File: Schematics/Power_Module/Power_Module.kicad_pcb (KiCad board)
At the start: 4 copper layers, 69.5 x 60 mm, 130 parts, among them J1 ScrewSwitch, J2 Battery, J3 ScrewSwitch, J4 GSE, J5 USB_C_Female_USB2_Small, J6 SWD_B, J7 Stack Male Edge Connector, Q1 AO4447A, Q2 TSM2309CX, Q3 DMN6040SSD-13, SW1 SW_STM_RESET, SW2 SW_STM_BOOT_MODE, U1 TPS61175PWPR, U10 LM66100DCKR, U11 LM66100DCKR, U12 AMS1117-3.3, U13 CP2102N-A02-GQFN20R, U14 STM32F103CBT6, U15 ISO1044BDR, U16 W25Q128JVS, U2 LM74700QDBVRQ1, U3 LM74700QDBVRQ1, U4 ACS37041KLHBLT-010B3, U5 ACS37041KLHBLT-010B5, U6 INA181A2, U7 LMR51430XDDCR, U8 LMR51430XDDCR, U9 LM66100DCKR, Y1 X322516MMB4SI

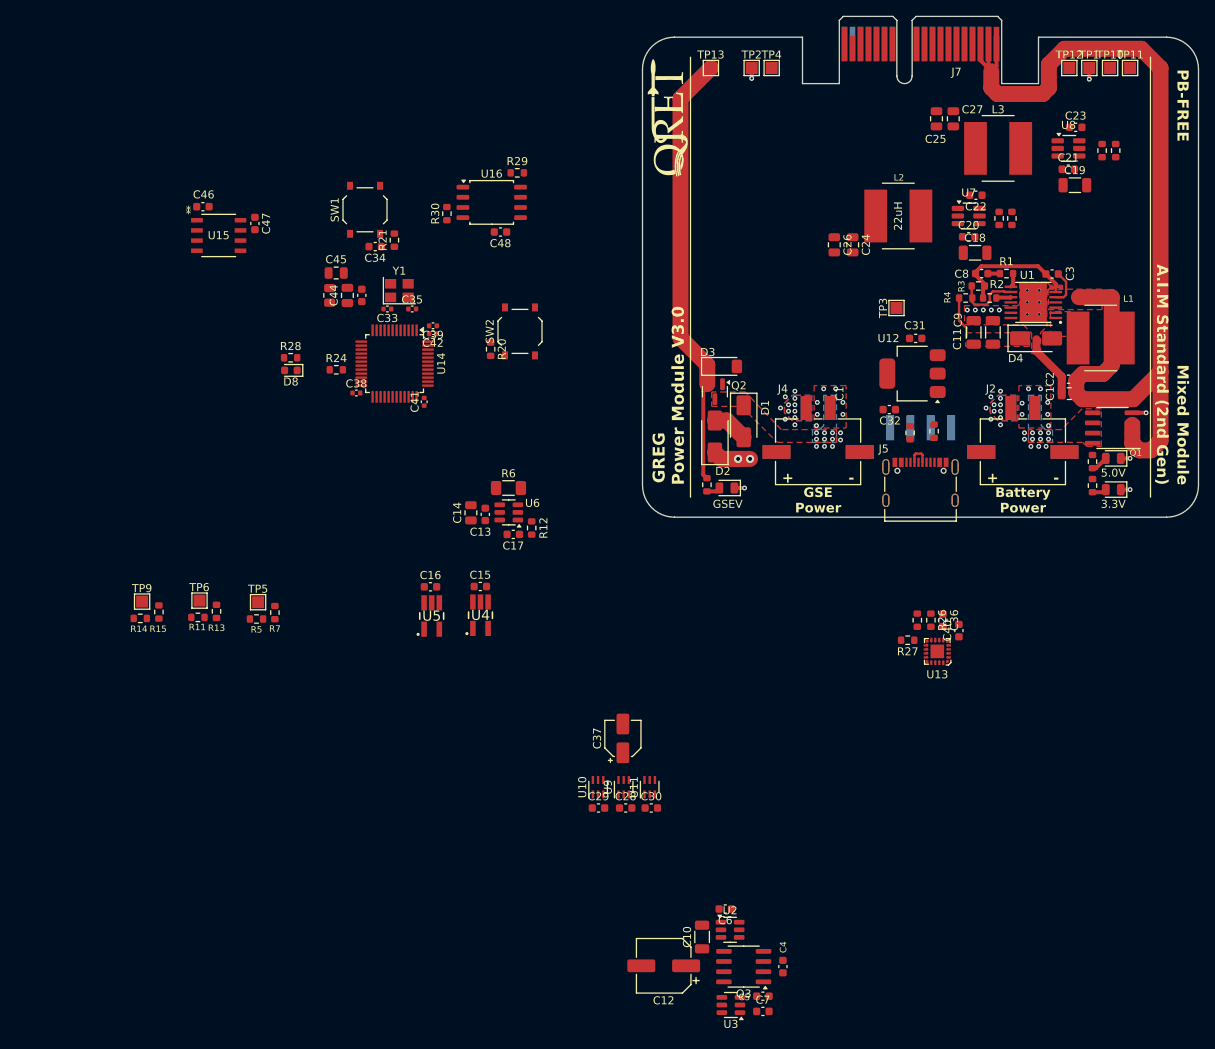
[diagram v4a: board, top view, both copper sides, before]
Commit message: continueing layout, confirmed all devices will fix  - need to add bulk rail caps  - fixed issue in oring logic
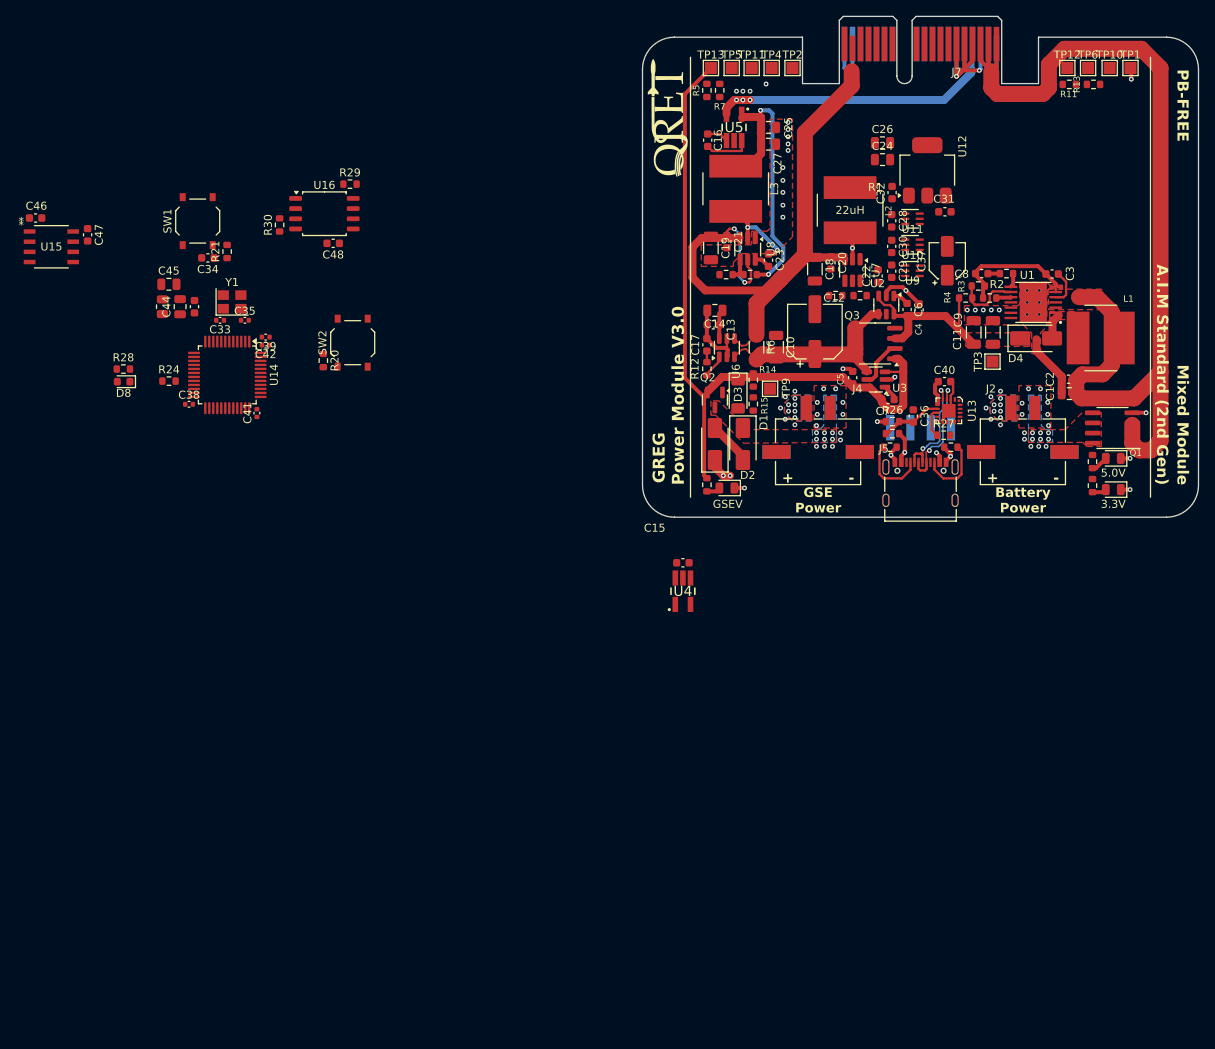
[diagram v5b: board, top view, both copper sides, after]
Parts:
- moved TP6 129.5 mm to (185.9, 43.6)
- moved R13 127.9 mm to (186.6, 45.6), turned to 0 degrees
- moved R11 127.7 mm to (183.6, 45.6)
- moved TP5 89.2 mm to (141.4, 43.6)
- moved R5 86.8 mm to (138.3, 46.4), turned to 90 degrees
- moved R7 85.7 mm to (139.9, 46.4)
- moved C4 83.8 mm to (164.8, 73.8), turned to -90 degrees
- moved TP9 82.9 mm to (146.2, 83.7), turned to 180 degrees
- moved R14 82.2 mm to (144.1, 82.6), turned to 90 degrees
- moved C12 81.5 mm to (151.8, 76.5), turned to 90 degrees
- moved C28 80.6 mm to (161.4, 62.7), turned to -90 degrees
- moved U2 80.5 mm to (160.7, 73.2), turned to -90 degrees
- moved U3 80.3 mm to (159.4, 82.5)
- moved U9 79.7 mm to (164.0, 62.5), turned to 0 degrees
- moved Q3 79.6 mm to (159.3, 78.0)
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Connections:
- net SWCLK_A renamed SWCLK
- net SWDIO_A renamed SWDIO
- C40 pad 1: GND -> 3.3V_MUX
- C40 pad 2: +3V3 -> GND
- C6 pad 1: GND -> Net-(U2-VCAP)
- C7 pad 2: GND -> Net-(U3-VCAP)
- J5 pad A6: USB_D+ -> USB_P
- J5 pad A7: USB_D- -> USB_N
- J5 pad B6: USB_D+ -> USB_P
- J5 pad B7: USB_D- -> USB_N
- R27 pad 2: +3V3 -> 3.3V_MUX
- U13 pad 6: +3V3 -> 3.3V_MUX
- U13 pad 7: +3V3 -> 3.3V_MUX
- U14 pad 30: TX_A -> unconnected-(U14-PA9-Pad30)
- U14 pad 31: RX_A -> unconnected-(U14-PA10-Pad31)
- U2 pad 1: 24V_PSU -> Net-(U2-VCAP)
- U3 pad 1: 24V_GSE -> Net-(U3-VCAP)
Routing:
- net 24V_MUX: track 0.00 -> 87.6 mm, vias 0 -> 2
- net GND: track 36.7 -> 90.9 mm, vias 47 -> 68
- net 5V_PSU: track 0.00 -> 43.0 mm, vias 0 -> 3
- net 24V_GSE: track 54.6 -> 90.8 mm
- net 5V_PSU_Pre: track 0.00 -> 36.0 mm, vias 0 -> 2
- net 24V_MUX_Pre: track 0.00 -> 29.0 mm
- net 24V_PSU: track 5.23 -> 24.4 mm
- net USB_N: track 0.00 -> 15.0 mm, vias 0 -> 2
- net USB_P: track 0.00 -> 14.9 mm, vias 0 -> 2
- net Net-(U8-SW): track 0.00 -> 10.2 mm, vias 0 -> 2
- net Net-(J5-CC1): track 0.00 -> 9.03 mm
- net Net-(J5-CC2): track 0.00 -> 8.64 mm
- net Net-(U13-VBUS): track 0.00 -> 7.74 mm
- net 3.3V_MUX: track 0.00 -> 6.87 mm
- net 3.3V_PSU: track 0.00 -> 6.50 mm
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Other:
- board text removed: "C1"

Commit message: confirm layout, confirm everything fits
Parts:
- moved D8 126.1 mm to (191.0, 72.1)
- moved R28 126.1 mm to (191.0, 70.5)
- moved R24 115.6 mm to (183.5, 56.0), turned to -90 degrees
- moved C33 112.5 mm to (188.5, 57.0)
- moved C35 112.5 mm to (191.6, 57.0)
- moved Y1 112.5 mm to (190.0, 54.6)
- moved C34 111.6 mm to (186.1, 49.6), turned to -90 degrees
- moved C38 110.3 mm to (180.5, 58.4), turned to -90 degrees
- moved C39 108.6 mm to (191.3, 68.0), turned to 90 degrees
- moved C42 107.7 mm to (190.3, 68.0), turned to 90 degrees
- moved SW1 107.5 mm to (181.5, 50.8), turned to 180 degrees
- moved U14 107.5 mm to (184.2, 63.1), turned to 180 degrees
- moved R21 107.2 mm to (183.8, 47.2), turned to 180 degrees
- moved C43 105.4 mm to (176.9, 49.6)
- moved C44 105.4 mm to (175.8, 52.9)
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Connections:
- C46 pad 1: +3V3 -> 3.3V_MUX
- C47 pad 1: +5V -> 5V_PSU
- U15 pad 1: +3V3 -> 3.3V_MUX
- U15 pad 8: +5V -> 5V_PSU
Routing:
- net 3.3V_MUX: track 6.87 -> 145.2 mm, vias 0 -> 5
- net 3.3V_SWD: track 0.00 -> 48.4 mm, vias 0 -> 2
- net SWDIO: track 0.00 -> 42.2 mm, vias 0 -> 1
- net SWCLK: track 0.00 -> 40.1 mm, vias 0 -> 1
- net 3.3V_PSU: track 6.50 -> 43.7 mm, vias 0 -> 3
- net 3.3V_PSU_Pre: track 0.00 -> 33.7 mm, vias 0 -> 2
- net 5V_USB: track 5.42 -> 36.6 mm, vias 2 -> 6
- net 3.3V_REGUSB: track 0.00 -> 26.0 mm
- net 24V_MUX: track 87.6 -> 107.7 mm, vias 2 -> 7
- net GND: track 90.9 -> 102.0 mm, vias 68 -> 79
- net Net-(U7-SW): track 3.42 -> 9.25 mm, vias 1 -> 2
- net Net-(U7-FB): track 0.00 -> 5.14 mm
- net 5V_PSU_Pre: track 36.0 -> 32.2 mm
- net 3.3V_ACS_PWR: track 0.00 -> 2.03 mm
- net Net-(U7-CB): track 0.00 -> 1.82 mm
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- added copper zone on F.Cu, net 3.3V_REGUSB

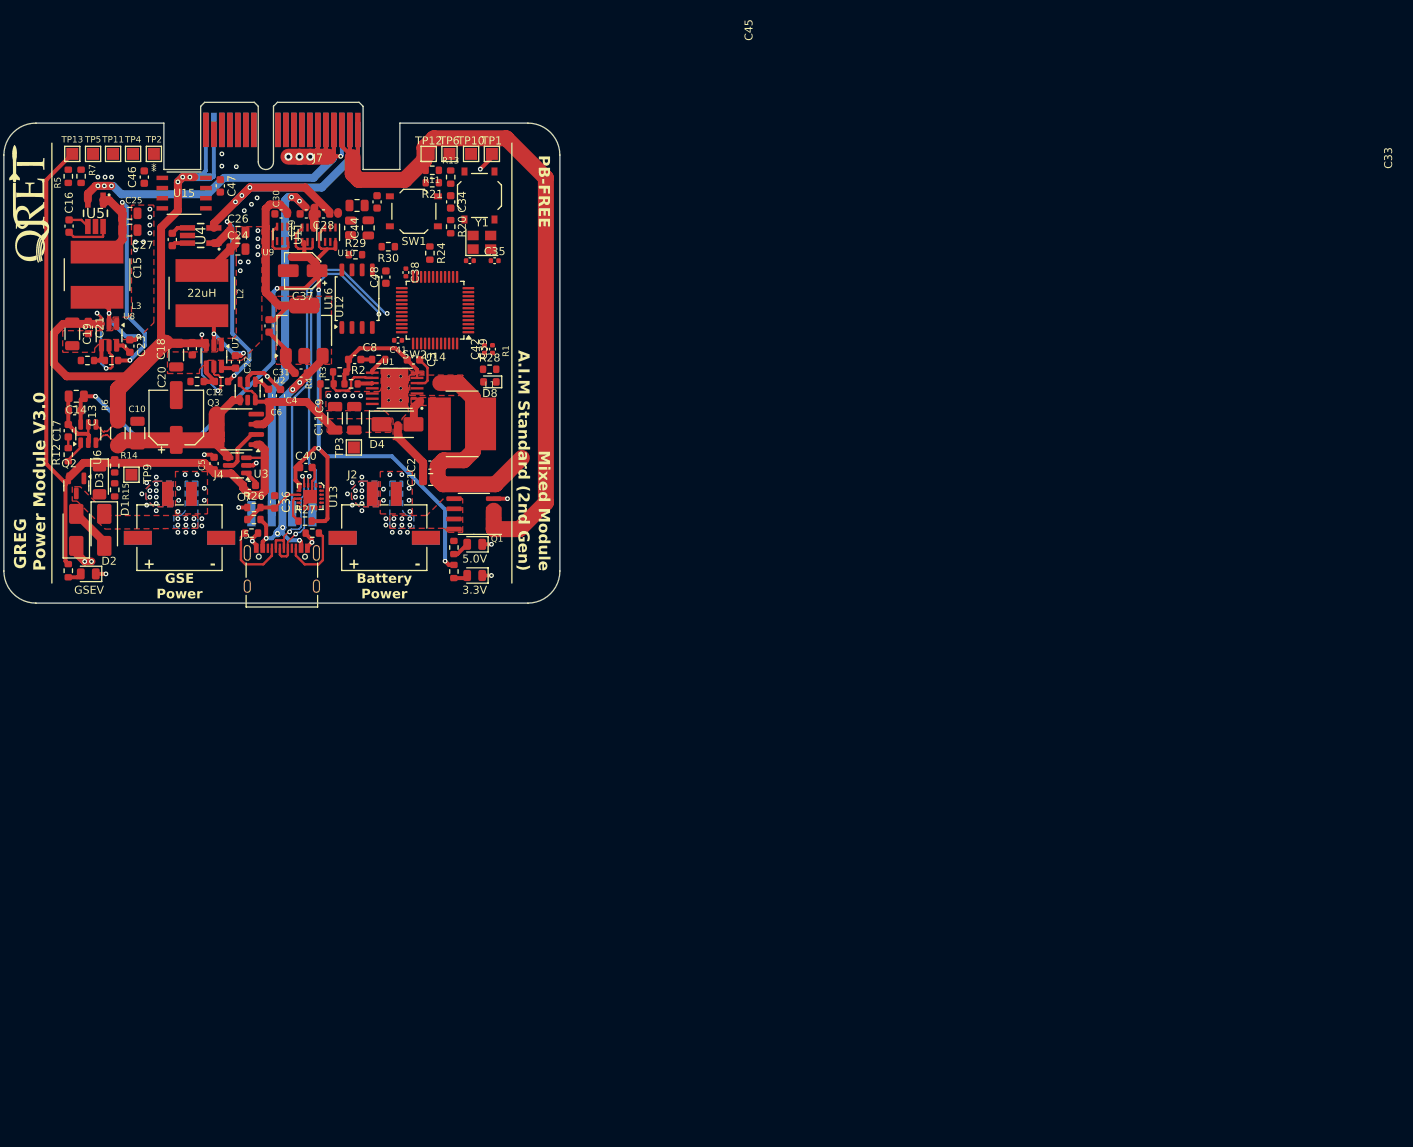
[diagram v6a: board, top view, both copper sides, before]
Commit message: completed all power traces, finalizing signal traces
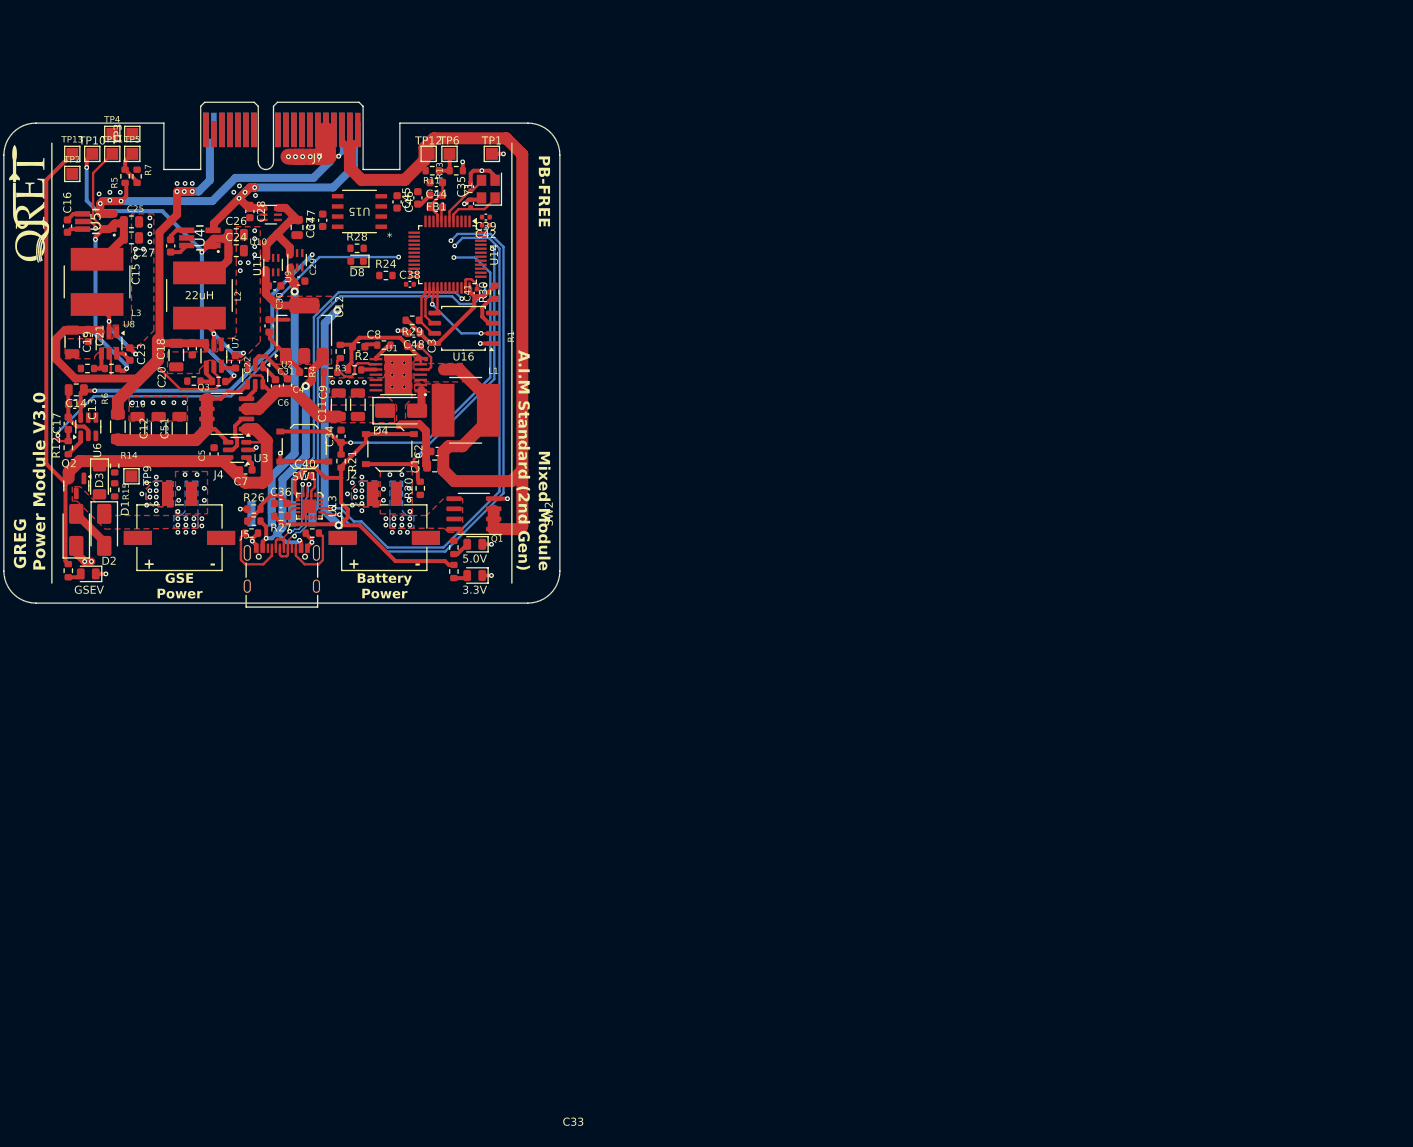
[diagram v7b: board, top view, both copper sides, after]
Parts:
- added C51: 22uF, Capacitor_SMD:C_1206_3216Metric, F.Cu at (152.2, 77.9)
- C12: value 100uF -> 22uF; footprint Capacitor_SMD:CP_Elec_6.3x5.9 -> Capacitor_SMD:C_1206_3216Metric
- C37: footprint Capacitor_SMD:CP_Elec_4x5.4 -> Capacitor_SMD:C_0805_2012Metric
- C44, C45: footprint Capacitor_SMD:C_0805_2012Metric -> Capacitor_SMD:C_0603_1608Metric
- FB1: footprint Resistor_SMD:R_0805_2012Metric -> Inductor_SMD:L_0603_1608Metric
- moved TP3 48.0 mm to (146.3, 41.1)
- moved TP10 47.3 mm to (141.3, 43.6)
- moved R21 36.6 mm to (172.4, 82.0), turned to -90 degrees
- moved SW2 33.6 mm to (178.5, 80.5), turned to 180 degrees
- moved R20 32.9 mm to (182.3, 85.4), turned to 90 degrees
- moved SW1 32.4 mm to (167.8, 80.2)
- moved C34 32.3 mm to (172.4, 78.9), turned to 90 degrees
- moved C46 31.8 mm to (179.4, 49.6), turned to 90 degrees
- moved D8 22.4 mm to (174.4, 57.0)
- moved R28 22.4 mm to (174.4, 55.4)
- moved U15 22.0 mm to (174.7, 50.8), turned to 180 degrees
- moved C39 16.5 mm to (190.5, 51.5), turned to 180 degrees
- moved C42 15.5 mm to (190.5, 52.5), turned to 180 degrees
- moved R30 14.5 mm to (191.6, 60.9), turned to 90 degrees
- moved U16 13.8 mm to (187.7, 65.4), turned to 180 degrees
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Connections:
- U1 pad 16: (no net) -> GND
- U1 pad 17: (no net) -> GND
- U1 pad 18: (no net) -> GND
- U1 pad 19: (no net) -> GND
- U1 pad 20: (no net) -> GND
- U1 pad 21: (no net) -> GND
- U14 pad 14: 3.3V_A_CURR_SENSE -> 3.3V_CURR_SENSE
- U14 pad 15: 5V_A_CURR_SENSE -> 5V_CURR_SENSE
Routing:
- net USART_TX: track 0.00 -> 66.2 mm, vias 0 -> 2
- net USART_RX: track 0.00 -> 64.2 mm, vias 0 -> 2
- net 24V_CURR_SENSE: track 1.40 -> 59.1 mm, vias 0 -> 2
- net STM_RESET: track 0.00 -> 50.0 mm, vias 0 -> 2
- net BOOT0: track 0.00 -> 39.7 mm, vias 0 -> 2
- net GND: track 102.0 -> 127.2 mm, vias 79 -> 91
- net 3.3V_PSU_Pre: track 33.7 -> 53.7 mm, vias 2 -> 3
- net 24V_MUX: track 107.7 -> 88.1 mm, vias 7 -> 3
- net 3.3V_SWD: track 48.4 -> 32.2 mm, vias 2 -> 1
- net 3.3V_REGUSB: track 26.0 -> 12.3 mm
- net 3.3V_MUX: track 145.2 -> 158.3 mm, vias 5 -> 4
- net MISO_FL: track 0.00 -> 11.1 mm, vias 0 -> 2
- net 5V_PSU_Pre: track 32.2 -> 41.8 mm
- net 3.3V_PSU: track 43.7 -> 34.2 mm
- net SWCLK: track 40.1 -> 48.6 mm
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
